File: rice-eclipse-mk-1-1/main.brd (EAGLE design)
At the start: 100 x 80 mm, 59 parts, among them IC1 LM7705, U1 LM1084ISX-5.0/NOPB, U2 THS4531IDRD8-M, U3 THS4531IDRD8-M, U4 THS4531IDRD8-M, U5 THS4531IDRD8-M, X1 2540-5

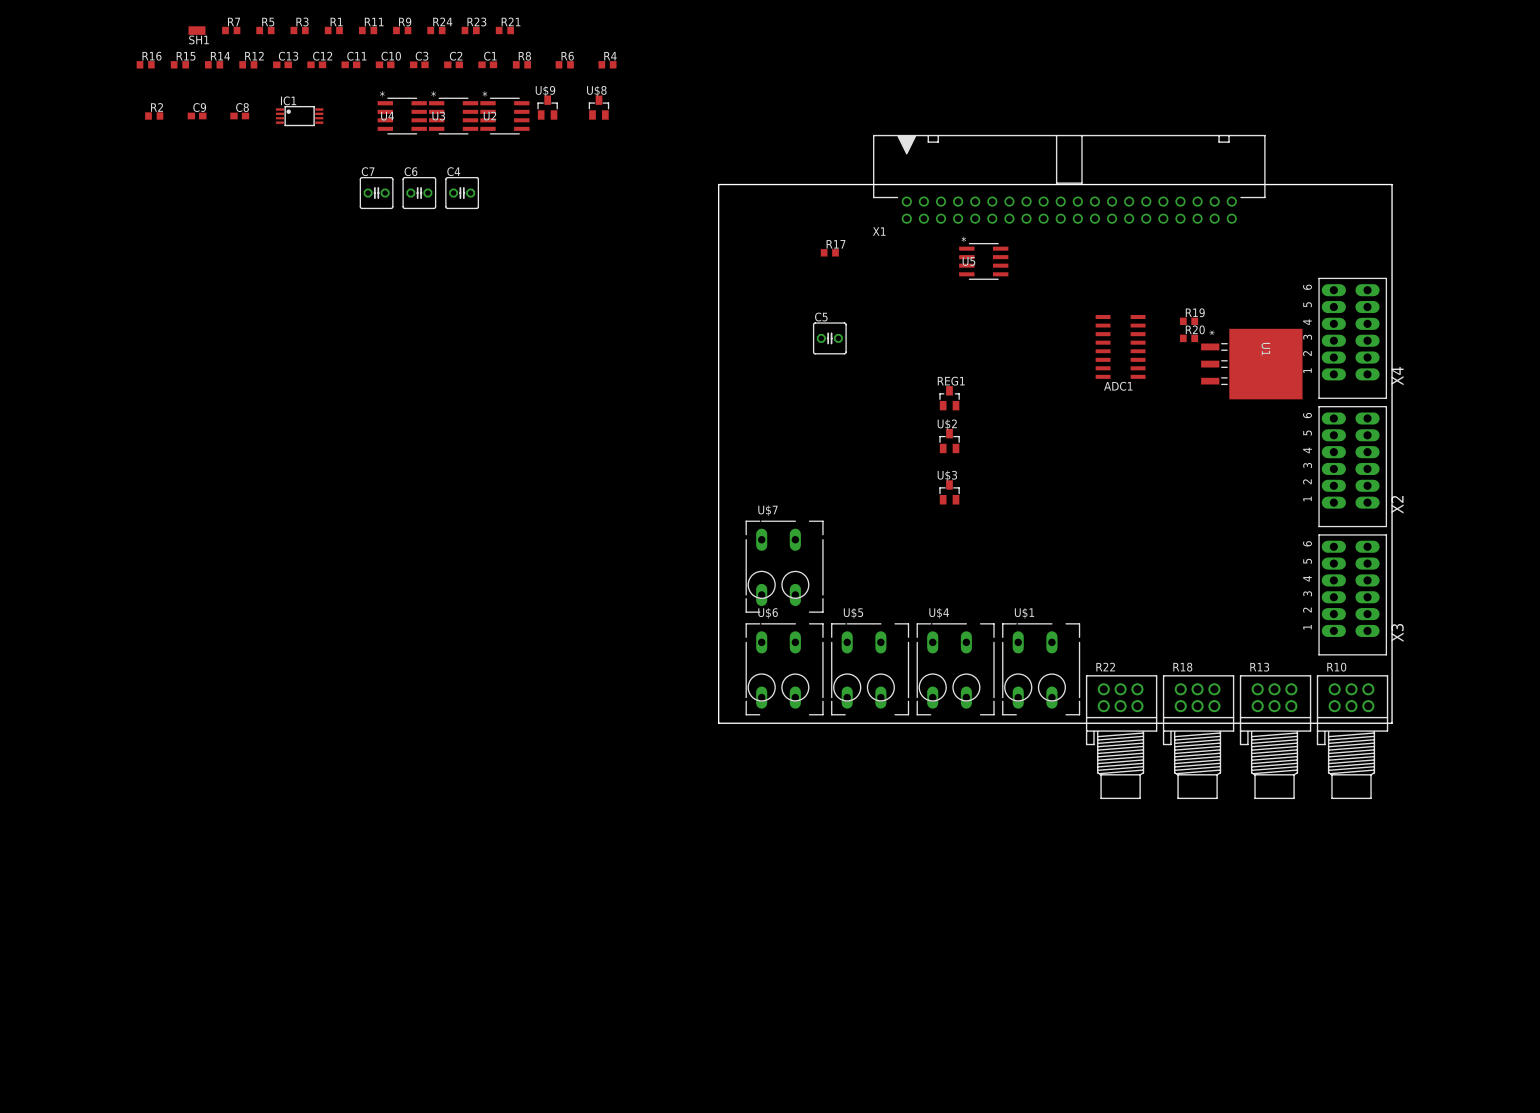
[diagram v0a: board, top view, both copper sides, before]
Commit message: Cleaned up placement on the board. Router scares me.
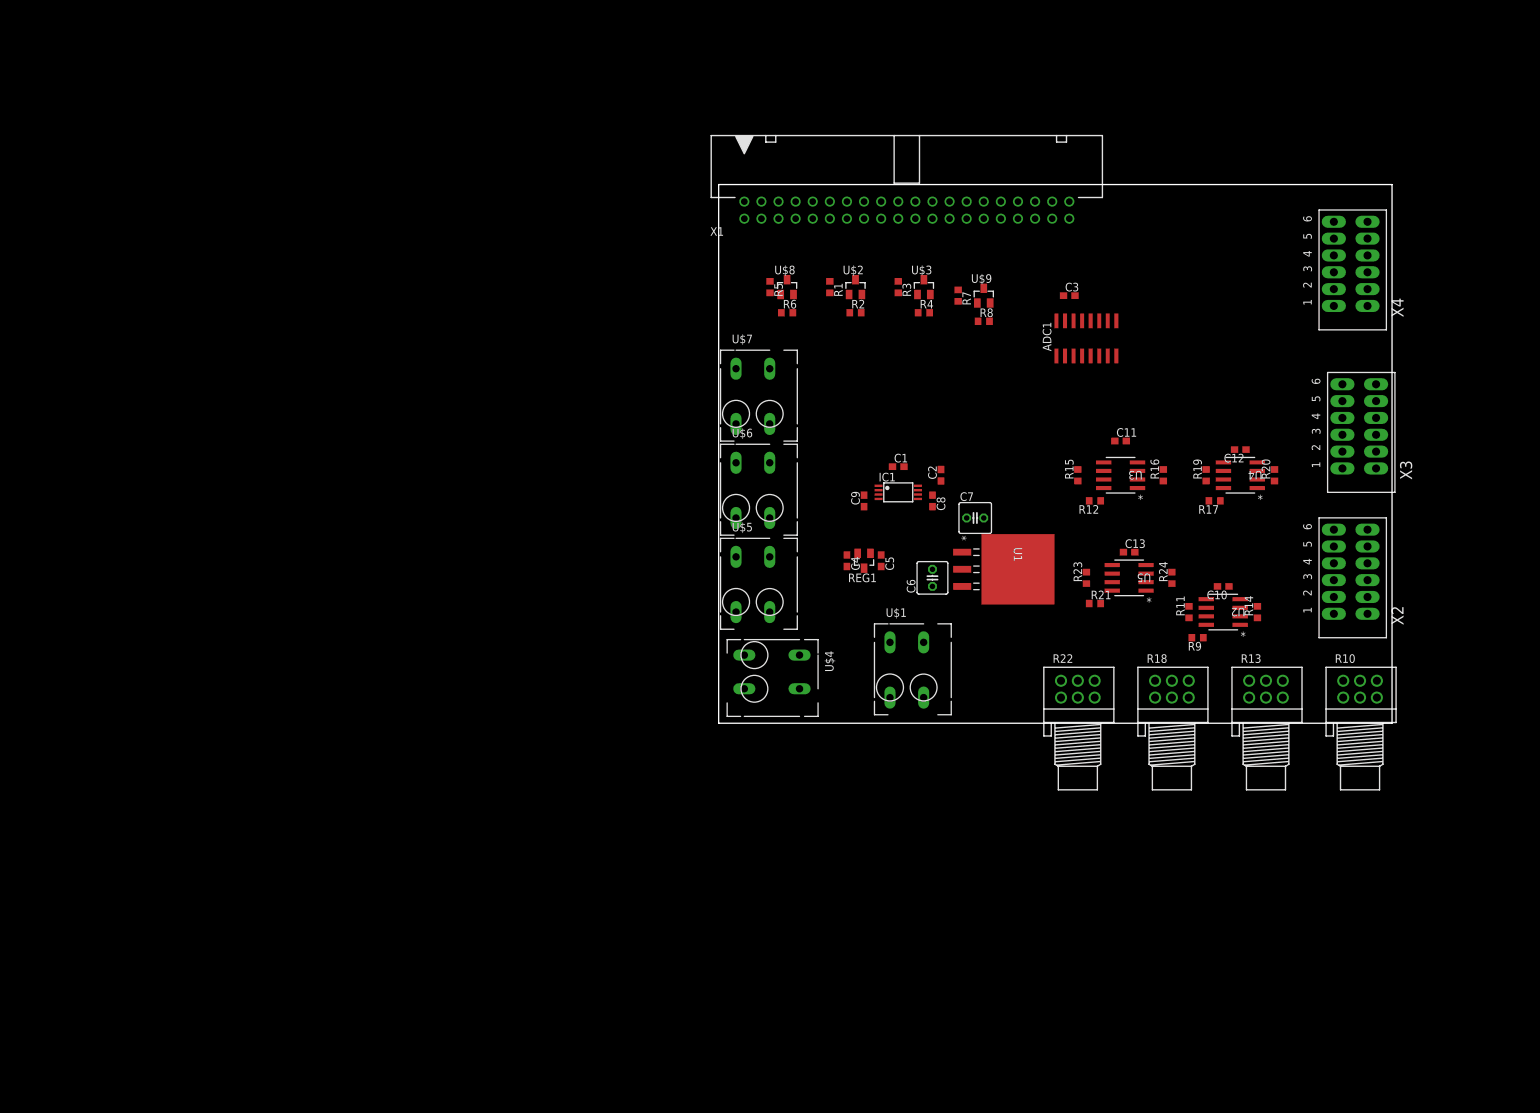
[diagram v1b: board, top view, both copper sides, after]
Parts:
- removed SH1: SHORTT5, shorts:SHORT_TOP-50
- C4: value 10UF -> 2.2UF; device rcl:C025-050X050 -> rcl:C0603
- C5: value 100UF -> 1UF; device rcl:C025-050X050 -> rcl:C0603
- moved R14 175.0 mm to (80.0, 16.5), turned to 90 degrees
- moved R16 163.0 mm to (66.0, 36.8), turned to 90 degrees
- moved R11 149.4 mm to (69.8, 16.5), turned to 90 degrees
- moved R9 148.6 mm to (71.1, 12.7), turned to 180 degrees
- moved C12 148.6 mm to (77.5, 40.6), turned to 180 degrees
- moved R15 146.6 mm to (53.3, 36.8), turned to 90 degrees
- moved C10 146.6 mm to (74.9, 20.3), turned to 180 degrees
- moved C13 145.1 mm to (61.0, 25.4)
- moved R12 141.4 mm to (55.9, 33.0), turned to 180 degrees
- moved R24 136.1 mm to (67.3, 21.6), turned to 90 degrees
- moved U4 135.4 mm to (77.5, 36.8), turned to 180 degrees
- moved U2 129.6 mm to (74.9, 16.5), turned to 180 degrees
- moved C11 127.2 mm to (59.7, 41.9)
- moved R23 122.3 mm to (54.6, 21.6), turned to 90 degrees
- moved R21 122.1 mm to (55.9, 17.8)
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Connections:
- removed net N$4: U1.4
- removed net TEST_NET_1: SH1.1
- removed net TEST_NET_2: SH1.2
- new net N$11: X4.P$11, X4.P$5
- net +5V: now also U1.4

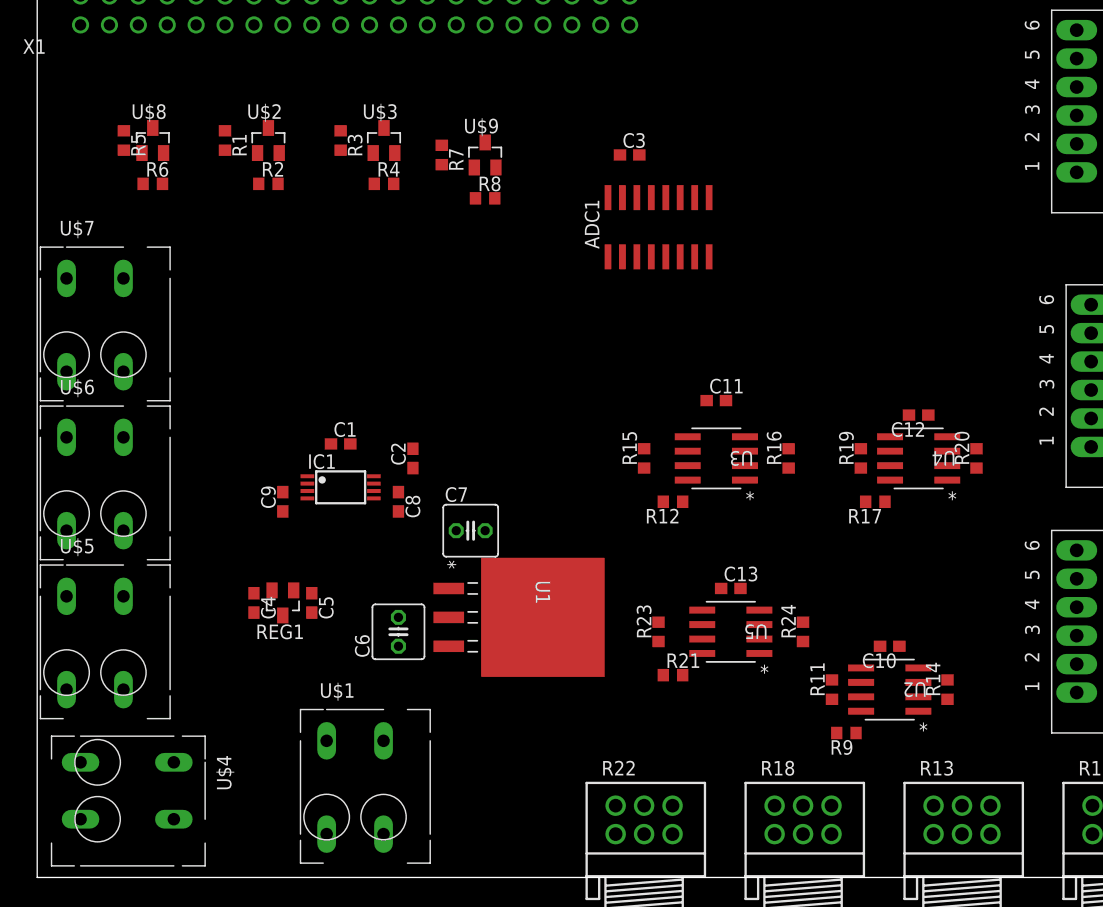
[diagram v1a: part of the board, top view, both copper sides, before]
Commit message: Added a new 4-pin signal connector. Also modified board.
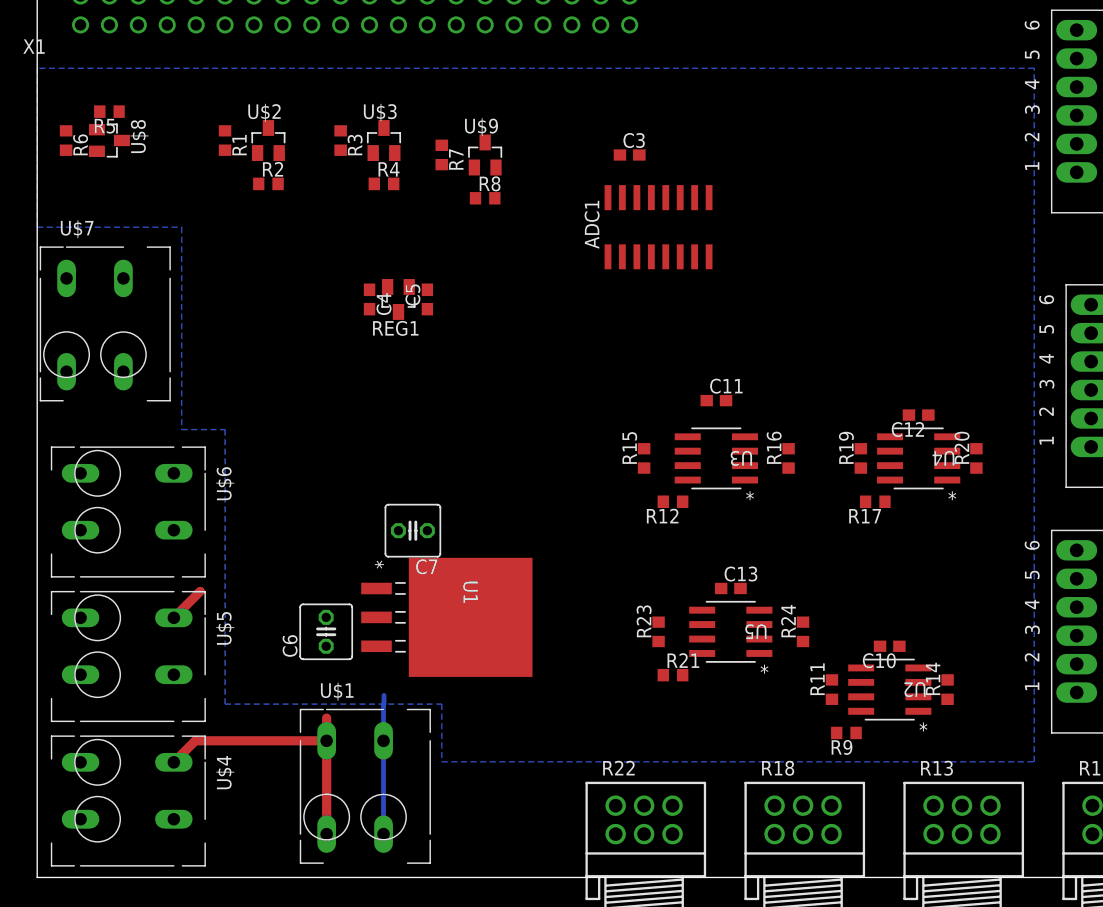
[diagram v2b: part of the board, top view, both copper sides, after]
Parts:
- removed C1, C2: 5UF, rcl:C0603
- removed C8: 22UF, rcl:C0603
- removed C9: 10UF, rcl:C0603
- removed IC1: LM7705, texas-extra:TSSOP8
- moved C4 28.5 mm to (29.2, 50.8)
- moved C5 28.5 mm to (34.3, 50.8), turned to 90 degrees
- moved REG1 28.5 mm to (31.8, 50.8)
- moved R6 8.52 mm to (2.54, 64.8), turned to 270 degrees
- moved C6 6.35 mm to (25.4, 21.6)
- moved U1 6.35 mm to (38.1, 22.9)
- moved C7 5.08 mm to (33.0, 30.5), turned to 180 degrees
- moved U$5 4.02 mm to (3.81, 20.3), turned to 270 degrees
- moved U$8 3.81 mm to (6.35, 64.8), turned to 270 degrees
- moved R5 2.84 mm to (6.35, 67.3), turned to 180 degrees
- moved U$6 2.84 mm to (3.81, 33.0), turned to 270 degrees
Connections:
- removed net -0V23: C10.2, C11.2, C12.2, C13.2, C8.1, IC1.6, U2.6, U3.6, U4.6, U5.6
- removed net AGND: ADC1.14, C3.2
- removed net DGND: ADC1.9
- removed net N$1: C1.1, IC1.1
- removed net N$2: C1.2, IC1.8
- removed net N$3: C2.1, IC1.7
- net +5V: no longer C9.1, IC1.4
- net GND: now also ADC1.14, ADC1.9, C10.2, C11.2, C12.2, C13.2, C3.2, U2.6, U3.6, U4.6, U5.6; no longer C2.2, C8.2, C9.2, IC1.2, IC1.3, IC1.5
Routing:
- net +12V: track 0.00 -> 24.4 mm
- net GND: track 0.00 -> 12.2 mm
- net +5V: track 0.00 -> 3.29 mm
- added copper zone on layer 16, net GND
